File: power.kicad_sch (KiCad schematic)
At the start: 55 parts, among them Q6 TSM085P03CV RGG, U17 INA3221AIRGV, U18 Analog LT8650SEV#PBF

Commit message: committing before attempting scripting
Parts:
- renumbered C145 to C144, C146 to C145, C147 to C146, C148 to C147, C149 to C148, C150 to C149, C151 to C150, C152 to C151, C153 to C152, C154 to C153, C155 to C154, C156 to C155, C157 to C156, C158 to C157, C159 to C158, C160 to C159, C161 to C160, C162 to C161, C163 to C162, Q6 to Q5, R107 to R100, R108 to R101, R109 to R102, R110 to R103, R111 to R104, R112 to R105, R113 to R106, R114 to R107, R115 to R108, R116 to R109, R117 to R110, R118 to R111, R119 to R112, R120 to R113, R121 to R114, R122 to R115, R123 to R116, R124 to R117, R101 to R94, R102 to R95, R103 to R96, R104 to R97, R105 to R98, R106 to R99

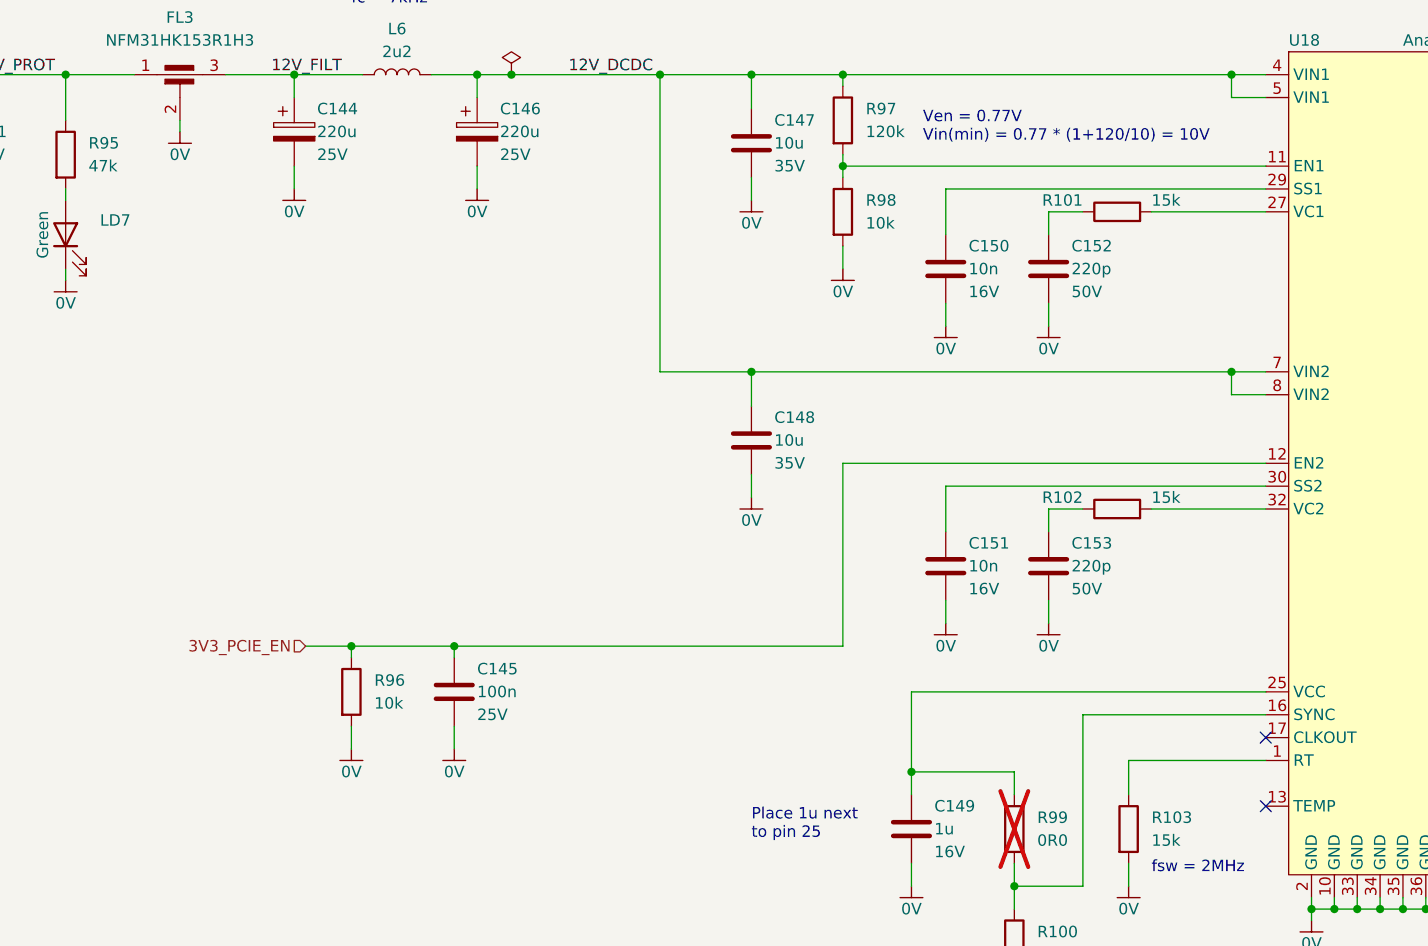
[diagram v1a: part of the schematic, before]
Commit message: Fixed connector offsets
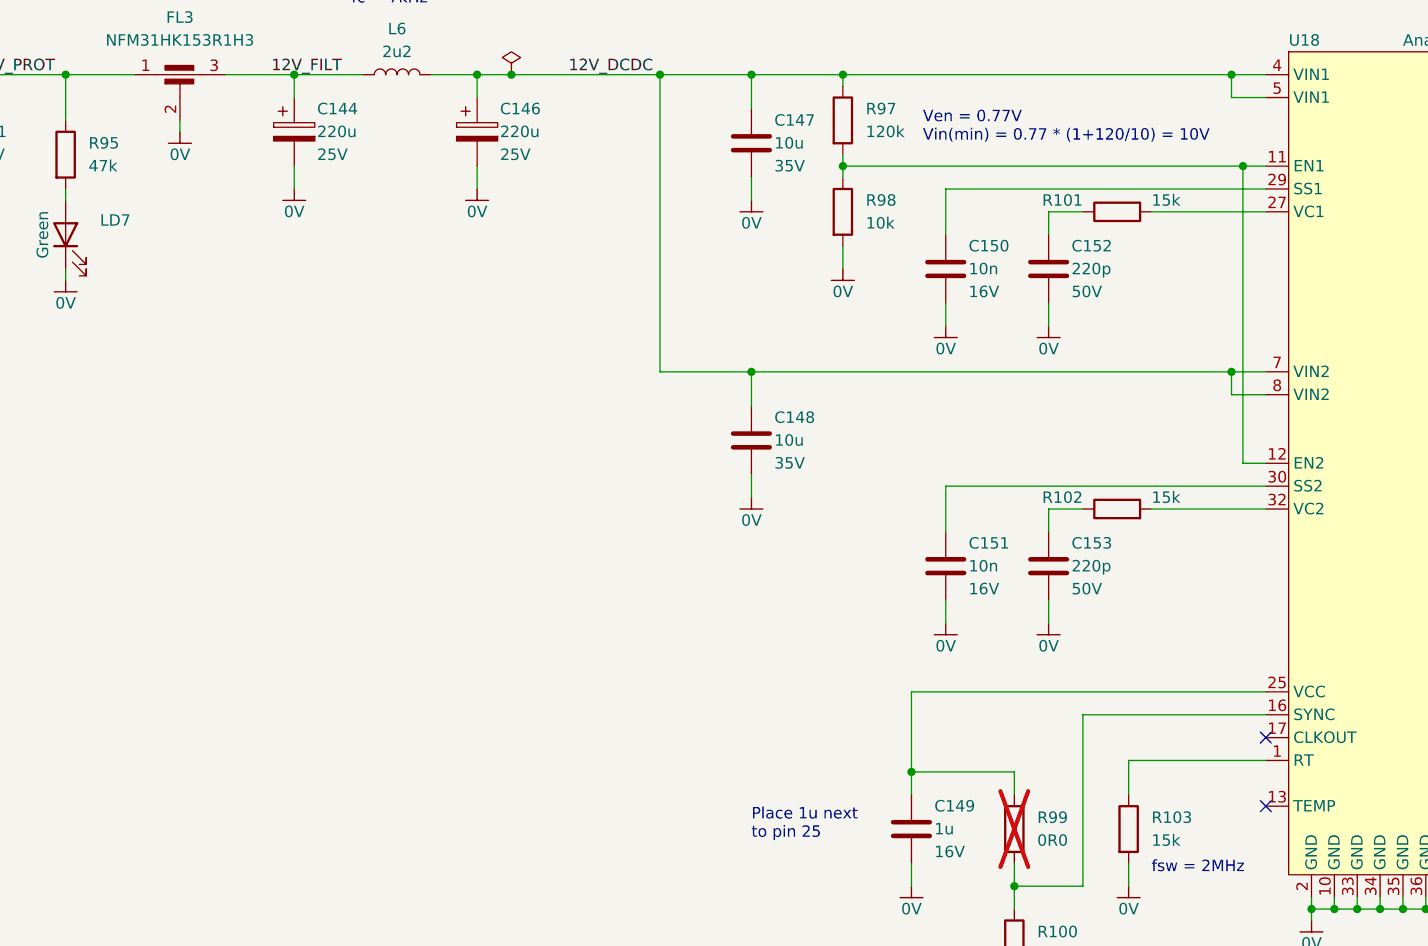
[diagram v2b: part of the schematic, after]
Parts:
- removed C145: 100n, Capacitor_SMD:C_0402_1005Metric, symbol AAA_Preferred_WUT:Yageo CC0402KRX7R8BB104
- removed R96: 10k, Resistor_SMD:R_0402_1005Metric, symbol AAA_Preferred_WUT:KOA Speer RK73H1ETTP1002F
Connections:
- net 3V3_PCIE_EN is gone; now on an unnamed net: U18.12 (EN2)
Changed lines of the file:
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@@
   (junction (at 358.14 88.9) (diameter 0) (color 0 0 0 0)
   )
+  (junction (at 203.2 66.04) (diameter 0) (color 0 0 0 0)
+  )
   (junction (at 39.37 50.8) (diameter 0) (color 0 0 0 0)
   )
@@
   (junction (at 121.92 55.88) (diameter 0) (color 0 0 0 0)
   )
-  (junction (at 104.14 119.38) (diameter 0) (color 0 0 0 0)
-  )
   (junction (at 39.37 53.34) (diameter 0) (color 0 0 0 0)
   )
@@
   (junction (at 148.59 88.9) (diameter 0) (color 0 0 0 0)
   )
-  (junction (at 115.57 119.38) (diameter 0) (color 0 0 0 0)
-  )
   (junction (at 266.7 140.97) (diameter 0) (color 0 0 0 0)
   )
@@
     (stroke (width 0) (type default))
   )
+  (wire (pts (xy 203.2 66.04) (xy 205.74 66.04))
+    (stroke (width 0) (type default))
+  )
   (wire (pts (xy 327.66 76.2) (xy 327.66 77.47))
     (stroke (width 0) (type default))
@@
     (stroke (width 0) (type default))
   )
-  (wire (pts (xy 115.57 119.38) (xy 158.75 119.38))
-    (stroke (width 0) (type default))
-  )
   (wire (pts (xy 238.76 58.42) (xy 238.76 60.96))
     (stroke (width 0) (type default))
@@
     (stroke (width 0) (type default))
   )
-  (wire (pts (xy 104.14 119.38) (xy 104.14 120.65))
-    (stroke (width 0) (type default))
-  )
   (wire (pts (xy 29.21 55.88) (xy 39.37 55.88))
     (stroke (width 0) (type default))
@@
     (stroke (width 0) (type default))
   )
-  (wire (pts (xy 99.06 119.38) (xy 104.14 119.38))
-    (stroke (width 0) (type default))
-  )
   (wire (pts (xy 113.03 55.88) (xy 118.11 55.88))
     (stroke (width 0) (type default))
@@
     (stroke (width 0) (type default))
   )
+  (wire (pts (xy 203.2 99.06) (xy 205.74 99.06))
+    (stroke (width 0) (type default))
+  )
   (wire (pts (xy 358.14 35.56) (xy 358.14 34.29))
     (stroke (width 0) (type default))
@@
     (stroke (width 0) (type default))
   )
-  (wire (pts (xy 158.75 119.38) (xy 158.75 99.06))
-    (stroke (width 0) (type default))
-  )
   (wire (pts (xy 187.96 208.28) (xy 207.01 208.28))
     (stroke (width 0) (type default))
@@
     (stroke (width 0) (type default))
   )
+  (wire (pts (xy 203.2 66.04) (xy 203.2 99.06))
+    (stroke (width 0) (type default))
+  )
   (wire (pts (xy 238.76 99.06) (xy 248.92 99.06))
     (stroke (width 0) (type default))
@@
     (stroke (width 0) (type default))
   )
-  (wire (pts (xy 158.75 66.04) (xy 205.74 66.04))
+  (wire (pts (xy 158.75 66.04) (xy 203.2 66.04))
     (stroke (width 0) (type default))
   )
@@
     (stroke (width 0) (type default))
   )
-  (wire (pts (xy 104.14 128.27) (xy 104.14 130.81))
-    (stroke (width 0) (type default))
-  )
   (wire (pts (xy 287.02 25.4) (xy 347.98 25.4))
     (stroke (width 0) (type default))
@@
     (stroke (width 0) (type default))
   )
-  (wire (pts (xy 158.75 99.06) (xy 205.74 99.06))
-    (stroke (width 0) (type default))
-  )
   (wire (pts (xy 261.62 109.22) (xy 261.62 111.76))
     (stroke (width 0) (type default))
@@
     (stroke (width 0) (type default))
   )
-  (wire (pts (xy 115.57 128.27) (xy 115.57 130.81))
-    (stroke (width 0) (type default))
-  )
   (wire (pts (xy 118.11 55.88) (xy 118.11 58.42))
     (stroke (width 0) (type default))
@@
     (stroke (width 0) (type default))
   )
-  (wire (pts (xy 115.57 119.38) (xy 104.14 119.38))
-    (stroke (width 0) (type default))
-  )
   (wire (pts (xy 327.66 58.42) (xy 327.66 59.69))
     (stroke (width 0) (type default))
@@
     (stroke (width 0) (type default))
   )
-  (wire (pts (xy 115.57 119.38) (xy 115.57 120.65))
-    (stroke (width 0) (type default))
-  )
   (wire (pts (xy 185.42 71.12) (xy 181.61 71.12))
     (stroke (width 0) (type default))
@@
     (effects (font (size 1.27 1.27)) (justify left))
   )
-  (hierarchical_label "3V3_PCIE_EN" (shape input) (at 99.06 119.38 180) (fields_autoplaced)
-    (effects (font (size 1.27 1.27)) (justify right))
-  )
   (symbol (lib_id "AAA_Preferred_WUT:KOA Speer RK73H1ETTP1003F") (at 266.7 134.62 0) (unit 1)
     (in_bom yes) (on_board yes) (dnp no)
@@
     )
   )
-  (symbol (lib_id "AAA_Preferred_WUT:KOA Speer RK73H1ETTP1002F") (at 104.14 124.46 0) (unit 1)
-    (in_bom yes) (on_board yes) (dnp no) (fields_autoplaced)
-    (property "Reference" "R96" (at 106.68 123.19 0)
-      (effects (font (size 1.27 1.27)) (justify left))
-    )
-    (property "Value" "10k" (at 106.68 125.73 0)
-      (effects (font (size 1.27 1.27)) (justify left))
-    )
-    (property "Footprint" "Resistor_SMD:R_0402_1005Metric" (at 102.362 124.46 90)
-      (effects (font (size 1.27 1.27)) hide)
-    )
-    (property "Datasheet" "https://www.koaspeer.com/pdfs/RK73H.pdf" (at 104.14 124.46 0)
-      (effects (font (size 1.27 1.27)) hide)
-    )
-    (property "MPN" "RK73H1ETTP1002F" (at 104.14 124.46 0)
-      (effects (font (size 1.27 1.27)) hide)
-    )
-    (property "Manufacturer" "KOA Speer" (at 104.14 124.46 0)
-      (effects (font (size 1.27 1.27)) hide)
-    )
-    (property "Tolerance" "1%" (at 104.14 124.46 0)
-      (effects (font (size 1.27 1.27)) hide)
-    )
-    (property "Height" "0.4mm" (at 104.14 124.46 0)
-      (effects (font (size 1.27 1.27)) hide)
-    )
-    (pin "1")
-    (pin "2")
-    (instances
-      (project "Master Timing Card"
-        (path "/6e8e281e-e30f-459d-852f-231836068db5/d6642cbe-acae-4c5e-b434-aaa25d469dab"
-          (reference "R96") (unit 1)
-        )
-      )
-    )
-  )
   (symbol (lib_id "Power_WUT:0V") (at 166.37 146.05 0) (unit 1)
     (in_bom no) (on_board no) (dnp no) (fields_autoplaced)
@@
     )
   )
-  (symbol (lib_id "Power_WUT:0V") (at 115.57 130.81 0) (unit 1)
-    (in_bom no) (on_board no) (dnp no) (fields_autoplaced)
-    (property "Reference" "#PWR0272" (at 115.57 130.81 0)
-      (effects (font (size 1.27 1.27)) hide)
-    )
-    (property "Value" "0V" (at 115.57 133.35 0) (do_not_autoplace)
-      (effects (font (size 1.27 1.27)))
-    )
-    (property "Footprint" "" (at 115.57 130.81 0)
-      (effects (font (size 1.27 1.27)) hide)
-    )
-    (property "Datasheet" "" (at 115.57 130.81 0)
-      (effects (font (size 1.27 1.27)) hide)
-    )
-    (pin "1")
-    (instances
-      (project "Master Timing Card"
-        (path "/6e8e281e-e30f-459d-852f-231836068db5/d6642cbe-acae-4c5e-b434-aaa25d469dab"
-          (reference "#PWR0272") (unit 1)
-        )
-      )
-    )
-  )
   (symbol (lib_id "Auto_Library_WUT:Coilcraft XEL4030-222MED") (at 251.46 58.42 90) (unit 1)
     (in_bom yes) (on_board yes) (dnp no) (fields_autoplaced)
@@
     )
   )
-  (symbol (lib_id "Power_WUT:0V") (at 104.14 130.81 0) (unit 1)
-    (in_bom no) (on_board no) (dnp no) (fields_autoplaced)
-    (property "Reference" "#PWR0271" (at 104.14 130.81 0)
-      (effects (font (size 1.27 1.27)) hide)
-    )
-    (property "Value" "0V" (at 104.14 133.35 0) (do_not_autoplace)
-      (effects (font (size 1.27 1.27)))
-    )
-    (property "Footprint" "" (at 104.14 130.81 0)
-      (effects (font (size 1.27 1.27)) hide)
-    )
-    (property "Datasheet" "" (at 104.14 130.81 0)
-      (effects (font (size 1.27 1.27)) hide)
-    )
-    (pin "1")
-    (instances
-      (project "Master Timing Card"
-        (path "/6e8e281e-e30f-459d-852f-231836068db5/d6642cbe-acae-4c5e-b434-aaa25d469dab"
-          (reference "#PWR0271") (unit 1)
-        )
-      )
-    )
-  )
   (symbol (lib_id "Fuse_WUT:Littelfuse_0467001.NR") (at 25.4 55.88 0) (unit 1)
     (in_bom yes) (on_board yes) (dnp no) (fields_autoplaced)
@@
         )
       )
-    )
-  )
-  (symbol (lib_id "AAA_Preferred_WUT:Yageo CC0402KRX7R8BB104") (at 115.57 124.46 0) (unit 1)
-    (in_bom yes) (on_board yes) (dnp no) (fields_autoplaced)
-    (property "Reference" "C145" (at 118.11 121.92 0) (do_not_autoplace)
-      (effects (font (size 1.27 1.27)) (justify left))
-    )
-    (property "Value" "100n" (at 118.11 124.46 0) (do_not_autoplace)
-      (effects (font (size 1.27 1.27)) (justify left))
-    )
-    (property "Footprint" "Capacitor_SMD:C_0402_1005Metric" (at 115.57 124.46 0)
-      (effects (font (size 1.27 1.27)) hide)
-    )
-    (property "Datasheet" "https://www.yageo.com/upload/media/product/productsearch/datasheet/mlcc/UPY-GPHC_X7R_6.3V-to-250V_23.pdf" (at 115.57 124.46 0)
-      (effects (font (size 1.27 1.27)) hide)
-    )
-    (property "Voltage" "25V" (at 118.11 127 0) (do_not_autoplace)
-      (effects (font (size 1.27 1.27) (color 0 100 100 1)) (justify left))
-    )
-    (property "Manufacturer" "Yageo" (at 115.57 124.46 0)
-      (effects (font (size 1.27 1.27)) hide)
-    )
-    (property "MPN" "CC0402KRX7R8BB104" (at 115.57 124.46 0)
-      (effects (font (size 1.27 1.27)) hide)
-    )
-    (property "Tolerance" "10%" (at 115.57 124.46 0)
-      (effects (font (size 1.27 1.27)) hide)
-    )
-    (property "Dielectric" "X7R" (at 115.57 124.46 0)
-      (effects (font (size 1.27 1.27)) hide)
-    )
-    (property "Height" "0.5mm" (at 115.57 124.46 0)
-      (effects (font (size 1.27 1.27)) hide)
-    )
-    (pin "2")
-    (pin "1")
-    (instances
-      (project "Master Timing Card"
-        (path "/6e8e281e-e30f-459d-852f-231836068db5/d6642cbe-acae-4c5e-b434-aaa25d469dab"
-          (reference "C145") (unit 1)
-        )
-      )

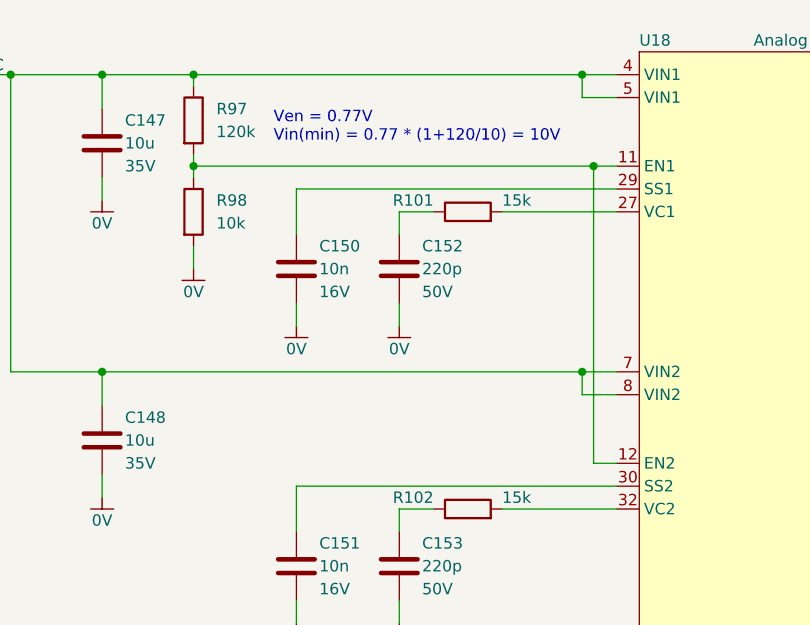
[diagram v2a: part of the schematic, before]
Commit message: Think complete - apart from 12V connection
Removed accidential step file
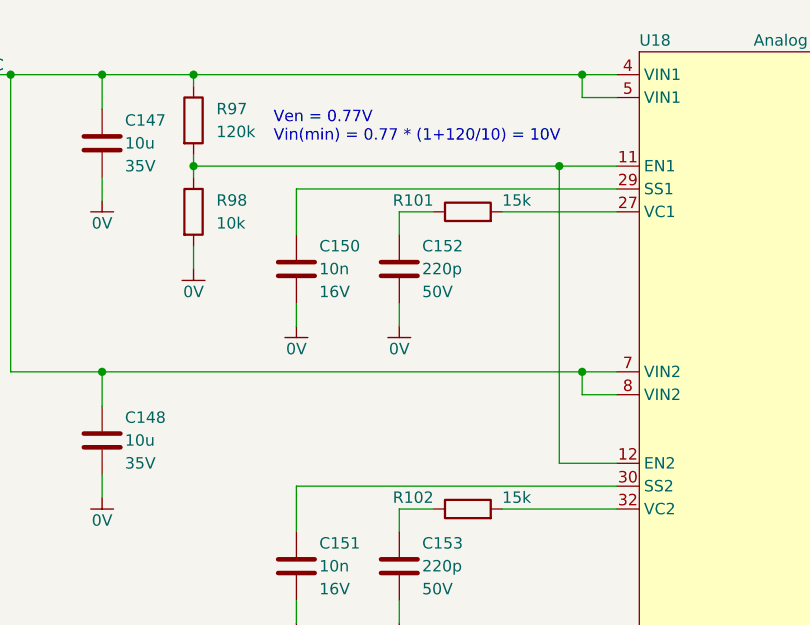
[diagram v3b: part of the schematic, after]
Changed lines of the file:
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@@
   (junction (at 358.14 88.9) (diameter 0) (color 0 0 0 0)
   )
-  (junction (at 203.2 66.04) (diameter 0) (color 0 0 0 0)
+  (junction (at 199.39 66.04) (diameter 0) (color 0 0 0 0)
   )
   (junction (at 39.37 50.8) (diameter 0) (color 0 0 0 0)
@@
     (stroke (width 0) (type default))
   )
-  (wire (pts (xy 203.2 66.04) (xy 205.74 66.04))
+  (wire (pts (xy 158.75 66.04) (xy 199.39 66.04))
     (stroke (width 0) (type default))
   )
@@
     (stroke (width 0) (type default))
   )
+  (wire (pts (xy 199.39 99.06) (xy 199.39 66.04))
+    (stroke (width 0) (type default))
+  )
   (wire (pts (xy 201.93 88.9) (xy 205.74 88.9))
     (stroke (width 0) (type default))
@@
     (stroke (width 0) (type default))
   )
-  (wire (pts (xy 203.2 99.06) (xy 205.74 99.06))
+  (wire (pts (xy 199.39 99.06) (xy 205.74 99.06))
     (stroke (width 0) (type default))
   )
@@
     (stroke (width 0) (type default))
   )
-  (wire (pts (xy 203.2 66.04) (xy 203.2 99.06))
-    (stroke (width 0) (type default))
-  )
   (wire (pts (xy 238.76 99.06) (xy 248.92 99.06))
     (stroke (width 0) (type default))
@@
     (stroke (width 0) (type default))
   )
-  (wire (pts (xy 158.75 66.04) (xy 203.2 66.04))
-    (stroke (width 0) (type default))
-  )
   (wire (pts (xy 97.79 55.88) (xy 97.79 58.42))
     (stroke (width 0) (type default))
@@
     (stroke (width 0) (type default))
   )
+  (wire (pts (xy 199.39 66.04) (xy 205.74 66.04))
+    (stroke (width 0) (type default))
+  )
